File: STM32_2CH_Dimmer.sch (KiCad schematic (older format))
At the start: 34 parts, among them J1 Power, J2 LED1, J3 Encoder1, J4 Encoder2, J5 LED2, Q1 IRF3708, Q2 IRF3708, SW1 Config, U1 LC78_03-05, U2 STM32F103Generic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

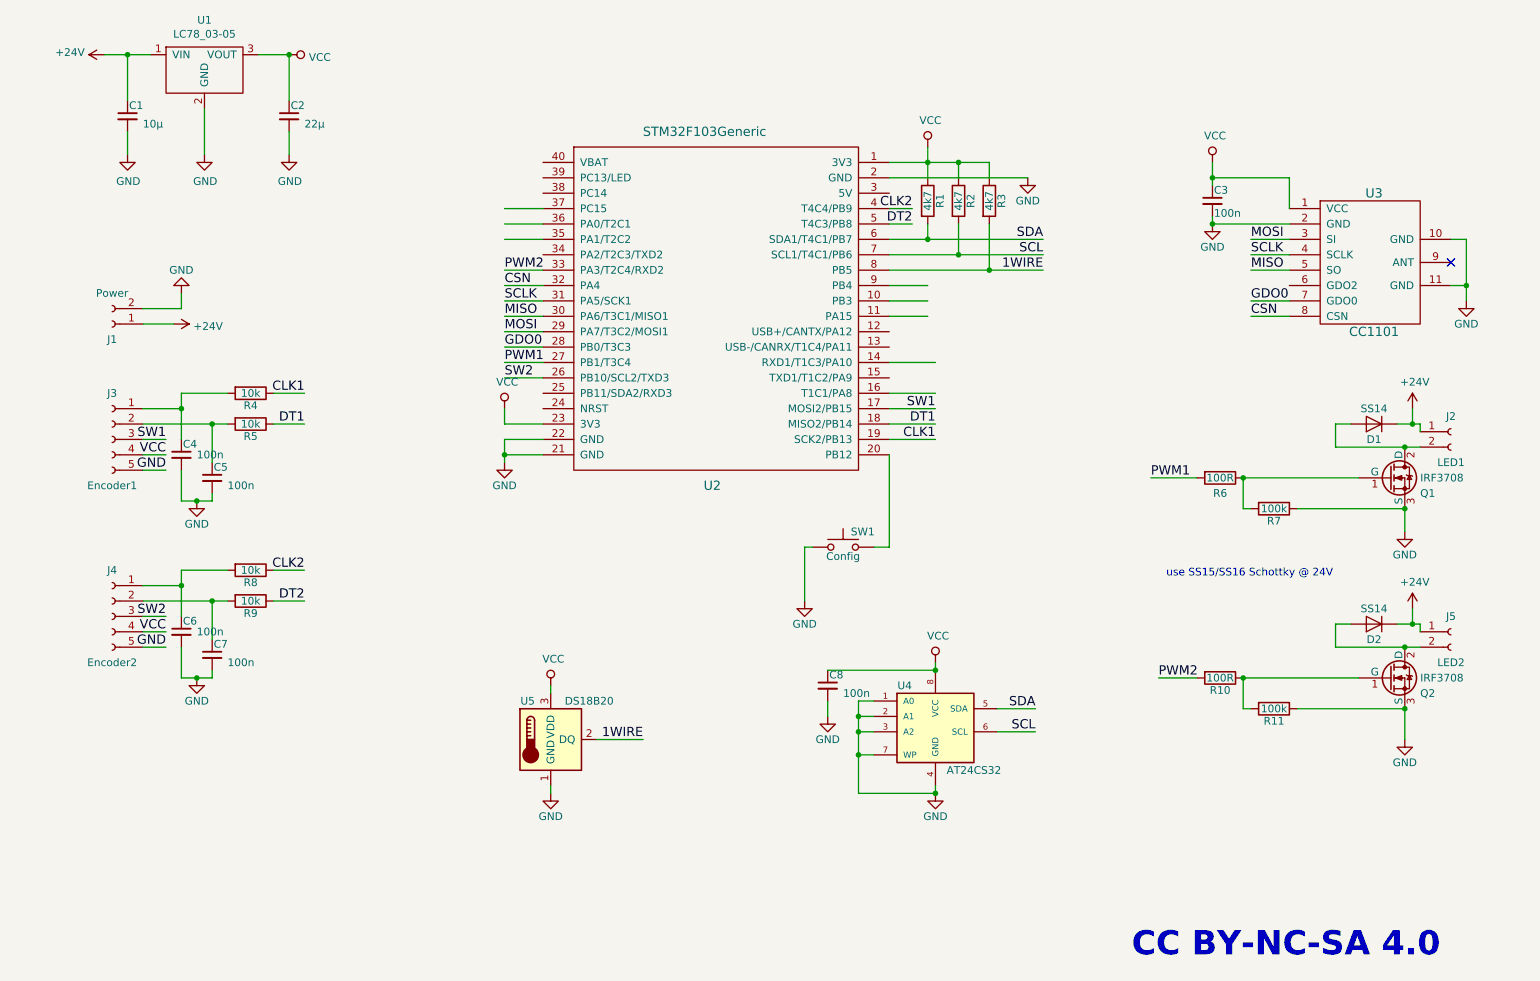
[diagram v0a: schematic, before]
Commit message: V1.3
minor fixes
add test pads for serial connection
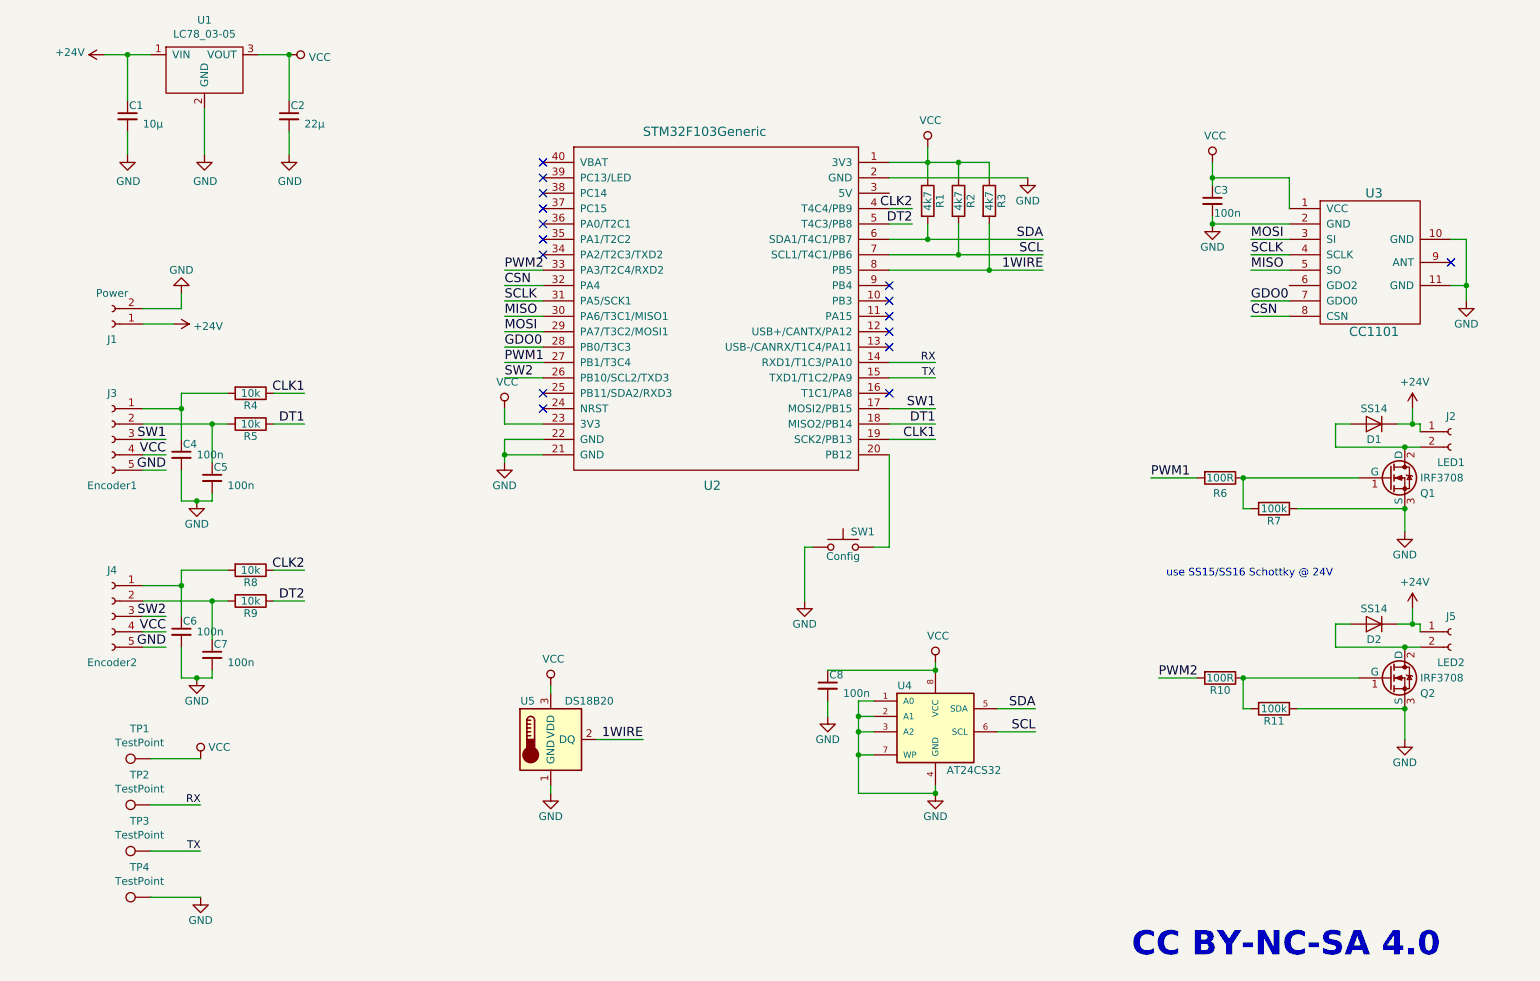
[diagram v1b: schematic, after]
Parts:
- added TP1, TP2, TP3, TP4: TestPoint, TestPoint:TestPoint_Pad_D1.5mm, symbol Connector:TestPoint
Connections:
- net labels added: RX, TX
- wire segments 152 -> 150
- no-connect marks 1 -> 16
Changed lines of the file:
@@
 Title "HM_STM32_2CH_Dimmer"
 Date ""
-Rev "V1.2"
+Rev "V1.3"
 Comp ""
 Comment1 ""
@@
 	9300 3600 9300 3450
 Wire Wire Line
-	6400 3250 6700 3250
-Wire Wire Line
 	9300 3450 9400 3450
 Wire Wire Line
@@
 	6300 5600 6200 5600
 Connection ~ 6200 5600
-Wire Wire Line
-	4150 2150 3900 2150
-Wire Wire Line
-	4150 2250 3900 2250
-Wire Wire Line
-	4150 2050 3900 2050
 Wire Wire Line
 	6850 1750 6850 1850
@@
 Wire Wire Line
 	6400 3050 6700 3050
-Wire Wire Line
-	6400 2750 6650 2750
-Wire Wire Line
-	6400 2650 6650 2650
-Wire Wire Line
-	6400 2550 6650 2550
 Wire Wire Line
 	4150 3150 3900 3150
@@
 Text Notes 8200 4450 0    50   ~ 0
 use SS15/SS16 Schottky @ 24V
+Wire Wire Line
+	6400 3150 6700 3150
+Text Label 6700 3050 2    50   ~ 0
+RX
+Text Label 6700 3150 2    50   ~ 0
+TX
+NoConn ~ 6400 2850
+NoConn ~ 6400 2950
+NoConn ~ 6400 3250
+NoConn ~ 4150 2350
+NoConn ~ 4150 2250
+NoConn ~ 4150 2150
+NoConn ~ 4150 2050
+NoConn ~ 4150 1950
+NoConn ~ 4150 1850
+NoConn ~ 4150 1750
+Wire Wire Line
+	1600 5625 1925 5625
+$Comp
+L power:VCC #PWR0102
+U 1 1 5DCD70B6
+P 1925 5625
+F 0 "#PWR0102" H 1925 5475 50  0001 C CNN
+F 1 "VCC" H 1975 5700 50  0000 L CNN
+F 2 "" H 1925 5625 50  0001 C CNN
+F 3 "" H 1925 5625 50  0001 C CNN
+	1    1925 5625
+	1    0    0    -1
+$EndComp
+Text Label 1925 6225 2    50   ~ 0
+TX
+Text Label 1925 5925 2    50   ~ 0
+RX
+Wire Wire Line
+	1600 6225 1925 6225
+Wire Wire Line
+	1600 5925 1925 5925
+$Comp
+L Connector:TestPoint TP1
+U 1 1 5DD0D09E
+P 1600 5625
+F 0 "TP1" V 1795 5697 50  0000 C CNN
+F 1 "TestPoint" V 1704 5697 50  0000 C CNN
+F 2 "TestPoint:TestPoint_Pad_D1.5mm" H 1800 5625 50  0001 C CNN
+F 3 "~" H 1800 5625 50  0001 C CNN
+	1    1600 5625
+	0    -1   -1   0
+$EndComp
+$Comp
+L Connector:TestPoint TP2
+U 1 1 5DD15DDC
+P 1600 5925
+F 0 "TP2" V 1795 5997 50  0000 C CNN
+F 1 "TestPoint" V 1704 5997 50  0000 C CNN
+F 2 "TestPoint:TestPoint_Pad_D1.5mm" H 1800 5925 50  0001 C CNN
+F 3 "~" H 1800 5925 50  0001 C CNN
+	1    1600 5925
+	0    -1   -1   0
+$EndComp
+$Comp
+L Connector:TestPoint TP3
+U 1 1 5DD1617F
+P 1600 6225
+F 0 "TP3" V 1795 6297 50  0000 C CNN
+F 1 "TestPoint" V 1704 6297 50  0000 C CNN
+F 2 "TestPoint:TestPoint_Pad_D1.5mm" H 1800 6225 50  0001 C CNN
+F 3 "~" H 1800 6225 50  0001 C CNN
+	1    1600 6225
+	0    -1   -1   0
+$EndComp
+$Comp
+L Connector:TestPoint TP4
+U 1 1 5DD16D49
+P 1600 6525
+F 0 "TP4" V 1795 6597 50  0000 C CNN
+F 1 "TestPoint" V 1704 6597 50  0000 C CNN
+F 2 "TestPoint:TestPoint_Pad_D1.5mm" H 1800 6525 50  0001 C CNN
+F 3 "~" H 1800 6525 50  0001 C CNN
+	1    1600 6525
+	0    -1   -1   0
+$EndComp
+Wire Wire Line
+	1600 6525 1925 6525
+$Comp
+L STM32_2CH_Dimmer-rescue:GND-STM32Dimmer-rescue #PWR0101
+U 1 1 5DCD6A8E
+P 1925 6525
+F 0 "#PWR0101" H 1925 6275 50  0001 C CNN
+F 1 "GND" H 1925 6375 50  0000 C CNN
+F 2 "" H 1925 6525 50  0001 C CNN
+F 3 "" H 1925 6525 50  0001 C CNN
+	1    1925 6525
+	1    0    0    -1
+$EndComp
+NoConn ~ 4150 3350
+NoConn ~ 4150 3250
+NoConn ~ 6400 2750
+NoConn ~ 6400 2650
+NoConn ~ 6400 2550
 $EndSCHEMATC

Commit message: info C1
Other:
- note added: "C1 is 10µF/50V !"
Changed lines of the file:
@@
 EESchema Schematic File Version 4
 LIBS:STM32_2CH_Dimmer-cache
-EELAYER 29 0
+EELAYER 30 0
 EELAYER END
 $Descr A4 11693 8268
@@
 F 1 "10µ" H 1550 1400 50  0000 L CNN
 F 2 "Capacitor_SMD:C_1210_3225Metric_Pad1.42x2.65mm_HandSolder" H 1450 1450 50  0001 C CNN
-F 3 "" H 1450 1450 50  0001 C CNN
+F 3 "https://de.aliexpress.com/item/2052321471.html" H 1450 1450 50  0001 C CNN
 	1    1450 1450
 	1    0    0    -1
@@
 NoConn ~ 6400 2650
 NoConn ~ 6400 2550
+Text Notes 700  2100 0    63   ~ 13
+C1 is 10µF/50V !
 $EndSCHEMATC

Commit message: update 1.4 final
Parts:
- removed C1: 10µ, Capacitor_SMD:C_1210_3225Metric_Pad1.42x2.65mm_HandSolder, symbol STM32_2CH_Dimmer-rescue:C_Small-STM32Dimmer-rescue
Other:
- note removed: "C1 is 10µF/50V !"
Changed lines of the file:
@@
 Title "HM_STM32_2CH_Dimmer"
 Date ""
-Rev "V1.3"
+Rev "V1.4"
 Comp ""
 Comment1 ""
@@
 	1    0    0    -1
 $EndComp
-$Comp
-L STM32_2CH_Dimmer-rescue:C_Small-STM32Dimmer-rescue C1
-U 1 1 5D987EF9
-P 1450 1450
-F 0 "C1" H 1460 1520 50  0000 L CNN
-F 1 "10µ" H 1550 1400 50  0000 L CNN
-F 2 "Capacitor_SMD:C_1210_3225Metric_Pad1.42x2.65mm_HandSolder" H 1450 1450 50  0001 C CNN
-F 3 "https://de.aliexpress.com/item/2052321471.html" H 1450 1450 50  0001 C CNN
-	1    1450 1450
-	1    0    0    -1
-$EndComp
-Wire Wire Line
-	1300 1050 1450 1050
-Wire Wire Line
-	1450 1350 1450 1050
-Connection ~ 1450 1050
-Wire Wire Line
-	1450 1050 1600 1050
-$Comp
-L power:GND #PWR04
-U 1 1 5D997FA2
-P 1450 1700
-F 0 "#PWR04" H 1450 1450 50  0001 C CNN
-F 1 "GND" H 1455 1527 50  0000 C CNN
-F 2 "" H 1450 1700 50  0001 C CNN
-F 3 "" H 1450 1700 50  0001 C CNN
-	1    1450 1700
-	1    0    0    -1
-$EndComp
-Wire Wire Line
-	1450 1700 1450 1550
 Text Notes 7975 6925 0    157  ~ 31
 CC BY-NC-SA 4.0
@@
 NoConn ~ 6400 2650
 NoConn ~ 6400 2550
-Text Notes 700  2100 0    63   ~ 13
-C1 is 10µF/50V !
+Wire Wire Line
+	1300 1050 1600 1050
 $EndSCHEMATC
